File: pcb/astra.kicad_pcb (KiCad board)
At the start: 4 copper layers, 49.2 x 45.5 mm, 93 parts, among them J1 Conn_01x02_Pin, J2 Conn_01x24_MountingPin, J3 Conn_02x04_Odd_Even, J4 Conn_02x05_Odd_Even, M1 Motor_DC, M2 Motor_DC, M3 Motor_DC, M4 Motor_DC, Q1 AO3400A, Q2 AO3400A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

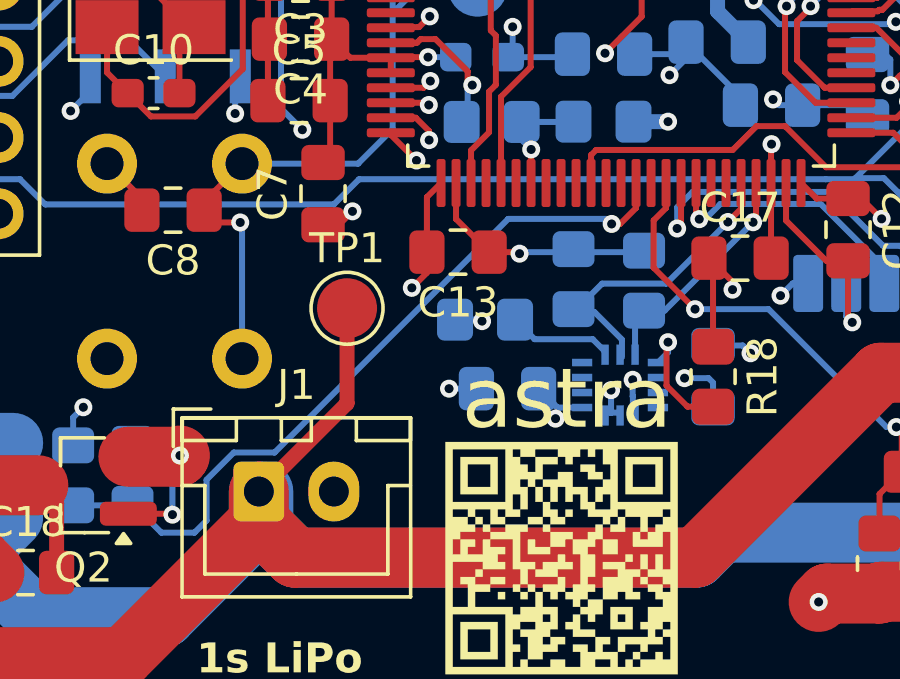
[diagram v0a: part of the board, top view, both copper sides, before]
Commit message: [pcb] add status led
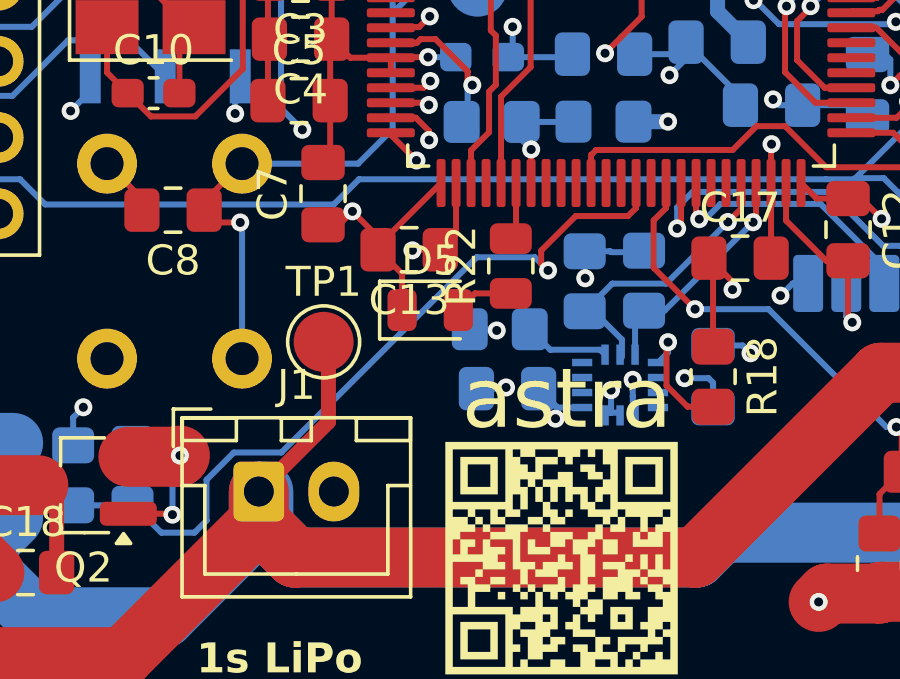
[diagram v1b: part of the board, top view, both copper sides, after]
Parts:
- added D5: LED, LED_SMD:LED_0805_2012Metric, F.Cu at (138.3, 66.6)
- added R22: 1k, Resistor_SMD:R_0805_2012Metric, F.Cu at (141.0, 65.2)
- moved C13 1.63 mm to (137.6, 64.6)
- moved TP1 1.36 mm to (134.7, 67.7)
- moved R19 0.59 mm to (140.6, 67.3)
- moved R17 0.38 mm to (143.4, 65.7)
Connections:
- U3 pad 31: unconnected-(U3-PA7-Pad31) -> STATUS_LED
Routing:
- net GND: track 126.4 -> 129.6 mm, vias 39 -> 38
- net Net-(D5-A): track 0.00 -> 1.98 mm
- net STATUS_LED: track 0.00 -> 1.93 mm
- net +BATT: track 253.5 -> 251.9 mm
- net +3.3V: track 79.6 -> 78.3 mm, vias 24 -> 25
- net MOTOR2: track 25.4 -> 26.4 mm
- net Net-(U7-CSB): track 3.64 -> 2.86 mm
- net IMU_SCL: track 30.1 -> 29.4 mm

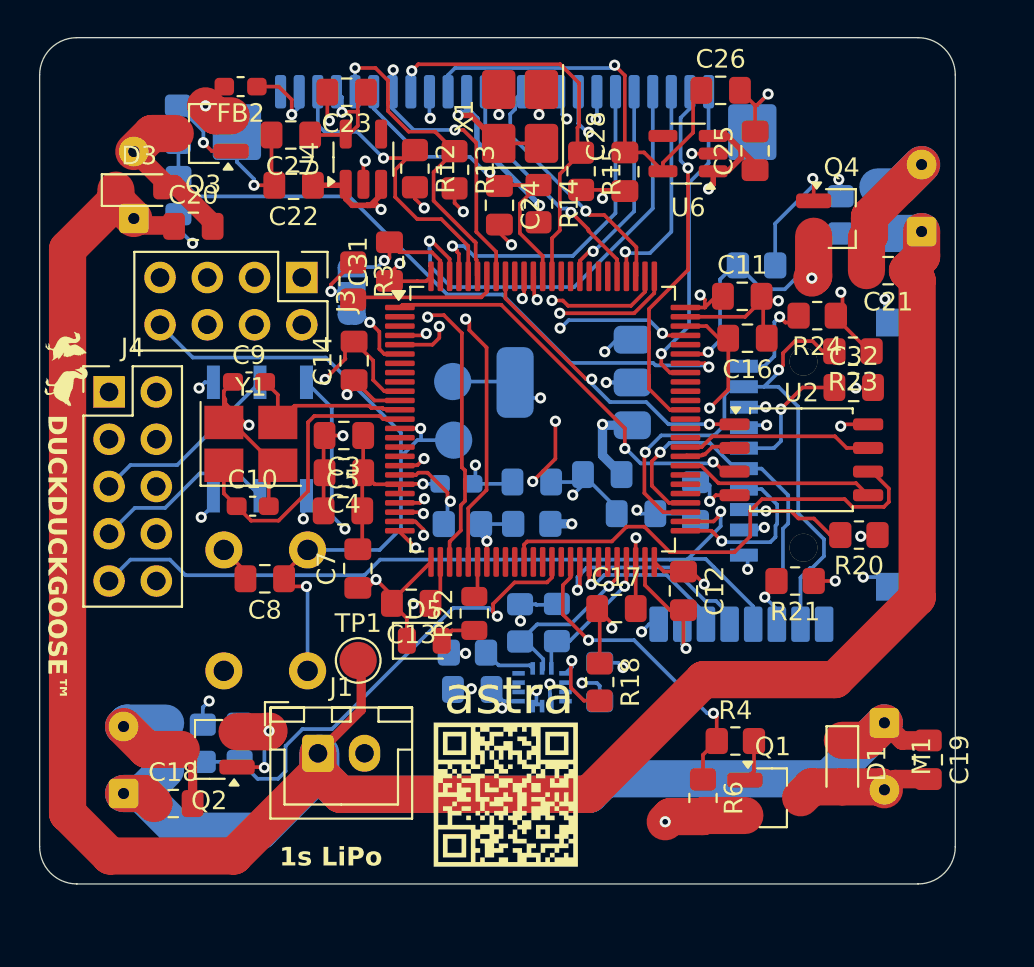
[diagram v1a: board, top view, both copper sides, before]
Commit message: [pcb] small fixes and improvements
- add two status LEDs
- move silkscreen labels for better visibility
- add more silkcreen logos/credits
- fix nrf footprint, add rf keepout zone
- add mounting holes
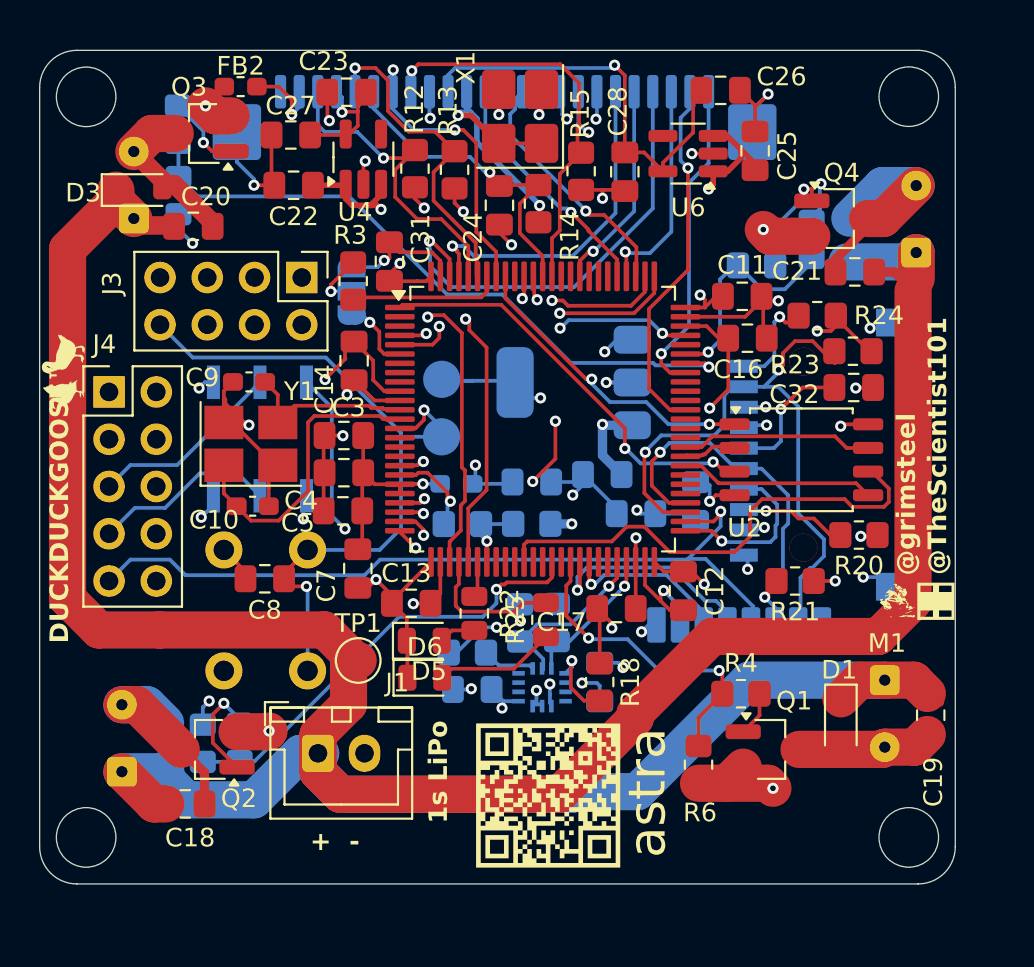
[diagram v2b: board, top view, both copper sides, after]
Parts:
- added D6: LED, LED_SMD:LED_0805_2012Metric, F.Cu at (138.3, 68.6)
- added G***: LOGO, LOGO, F.Cu at (165.8, 64.5)
- added G***: LOGO, LOGO, F.Cu at (163.6, 64.4)
- added G***: LOGO, LOGO, B.Cu at (135.0, 76.5)
- added R25: 1k, Resistor_SMD:R_0805_2012Metric, F.Cu at (144.8, 65.5)
- added REF**: MountingHole_3.2mm_M3, MountingHole:MountingHole_3.2mm_M3, F.Cu at (120.1, 37.4)
- added REF**: MountingHole_3.2mm_M3, MountingHole:MountingHole_3.2mm_M3, F.Cu at (164.3, 77.2)
- added REF**: MountingHole_3.2mm_M3, MountingHole:MountingHole_3.2mm_M3, F.Cu at (120.1, 77.2)
- added REF**: MountingHole_3.2mm_M3, MountingHole:MountingHole_3.2mm_M3, F.Cu at (164.3, 37.4)
- moved Q1 2.60 mm to (156.9, 72.5)
- moved R4 2.56 mm to (155.3, 69.5)
- moved C19 2.40 mm to (165.5, 70.6)
- moved M1 2.29 mm to (163.0, 68.8)
- moved QR***** 2.28 mm to (144.9, 75.0), turned to 90 degrees
- moved D4 2.26 mm to (161.0, 45.0)
- moved D1 2.23 mm to (160.7, 71.0)
- moved R11 2.04 mm to (159.1, 45.1)
- moved G*** 2.00 mm to (142.6, 75.9), turned to 90 degrees
- moved R6 1.81 mm to (153.0, 73.3)
- moved C21 1.79 mm to (161.4, 46.8)
- moved M2 1.17 mm to (122.0, 73.7)
- moved M4 1.17 mm to (164.7, 45.8)
- moved TP3 0.67 mm to (139.2, 55.7)
- moved C18 0.64 mm to (125.4, 75.4)
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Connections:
- net STATUS_LED renamed STATUS_LED_1
- U3 pad 29: unconnected-(U3-PA5-Pad29) -> STATUS_LED_2
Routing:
- net +BATT: track 251.9 -> 241.8 mm
- net STATUS_LED_2: track 0.00 -> 7.60 mm
- net Net-(D6-A): track 0.00 -> 6.48 mm
- net GND: track 129.6 -> 133.7 mm
- net +3.3V: track 78.3 -> 81.6 mm
- net MOTOR2: track 26.4 -> 24.1 mm
- net MOTOR4: track 14.6 -> 12.6 mm
- net Net-(D4-A): track 9.77 -> 11.2 mm
- net Net-(D2-A): track 9.11 -> 10.4 mm
- net Net-(Q2-G): track 4.39 -> 5.66 mm
- net RST: track 39.0 -> 40.1 mm
- net Net-(Q4-G): track 6.73 -> 5.77 mm
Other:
- board size 49.2 x 45.5 mm -> 49.2 x 44.8 mm
- board text added: "+ -"
- board text added: "0123abc"
- board text added: "@TheScientist101"
- board text added: "@grimsteel"
- board text added: "BOOT SELECT"
- board text added: "DDG PERIPHERAL"
- board text added: "I2C"
- board text added: "JLCJLCJLCJLC"
- board text added: "TDO TCK TMS RST"
- board text added: "TRST TDI GND 3V3"
- board text added: "github.com/TheScientist101/astra"
- board text removed: "I²C"

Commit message: [pcb] remove on-board camera
- remove camera and all supporting components (we'll be using an external dedicated board)
- extend DDG header
- make PCB smaller
- add more silkscreen labels
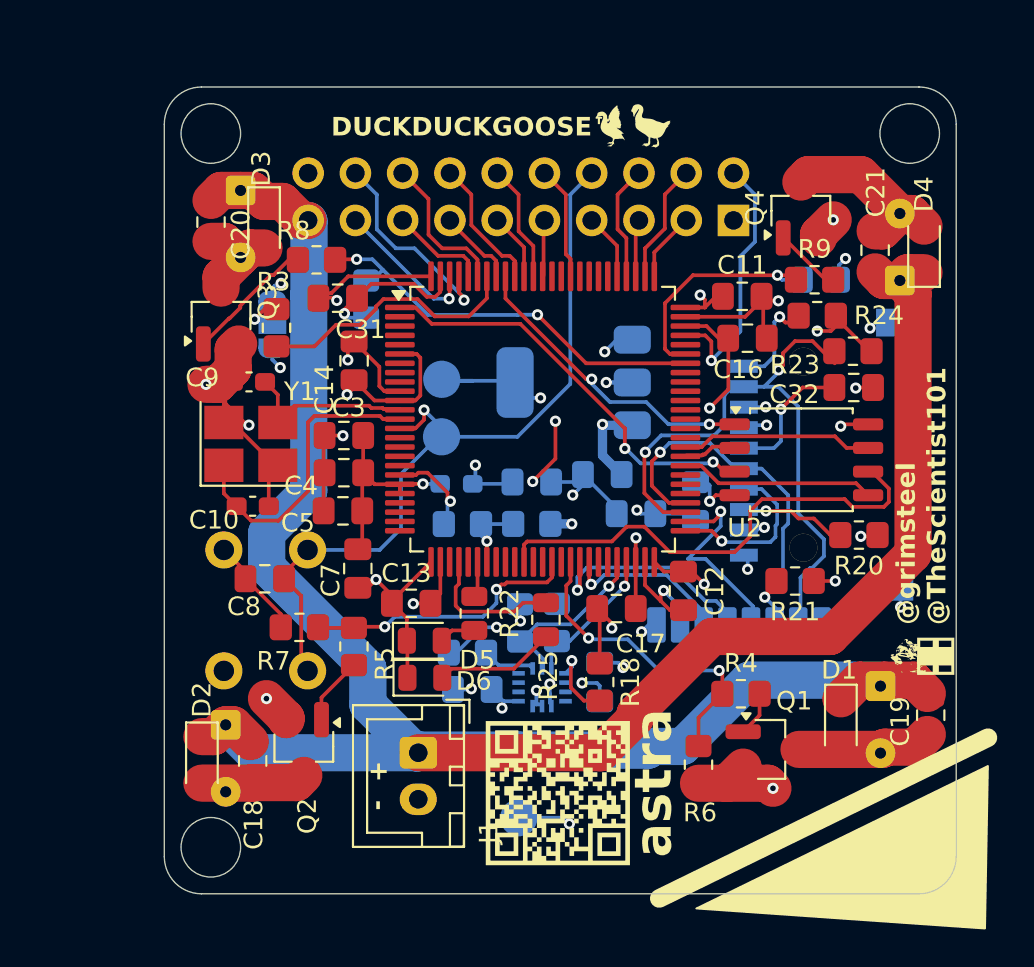
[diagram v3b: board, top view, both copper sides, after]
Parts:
- removed C22: 10uF, Capacitor_SMD:C_0805_2012Metric_Pad1.18x1.45mm_HandSolder
- removed C23, C25, C26: 1uF, Capacitor_SMD:C_0805_2012Metric_Pad1.18x1.45mm_HandSolder
- removed C24, C27, C28: 100nF, Capacitor_SMD:C_0805_2012Metric_Pad1.18x1.45mm_HandSolder
- removed FB2: 121T06, Inductor_SMD:L_0603_1608Metric_Pad1.05x0.95mm_HandSolder
- removed J3: Conn_02x04_Odd_Even, Connector_PinHeader_2.54mm:PinHeader_2x04_P2.54mm_Vertical
- removed J4: Conn_02x05_Odd_Even, Connector_PinHeader_2.54mm:PinHeader_2x05_P2.54mm_Vertical
- removed R12, R13, R14, R15: 10k, Resistor_SMD:R_0805_2012Metric_Pad1.20x1.40mm_HandSolder
- removed SW1: SS-3235S-L1, lcsc:SW-SMD_SS-3235S-LX
- removed U4: TLV74328PDBVR, Package_TO_SOT_SMD:SOT-23-5_HandSoldering
- removed U6: TLV74315PDBVR, Package_TO_SOT_SMD:SOT-23-5_HandSoldering
- removed X1: OT322524MJBA4SL, Crystal:Crystal_SMD_3225-4Pin_3.2x2.5mm_HandSoldering
- added G***: LOGO, LOGO, B.Cu at (157.6, 42.8)
- added GND: TP_GND, TestPoint:TestPoint_Pad_D2.0mm, B.Cu at (143.3, 76.1)
- D2, D4, R5, R7, R8, R9: moved to F.Cu
- J2: value Conn_01x24_MountingPin -> Conn_02x10_Odd_Even; footprint Connector_FFC-FPC:JUSHUO_AFA07-S24FCA-00_1x24-1MP_P1.0mm_Horizontal -> Connector_PinHeader_2.54mm:PinHeader_2x10_P2.54mm_Vertical
- M1: moved to B.Cu
- VCC: renamed from TP1; moved to B.Cu
- moved G*** 33.3 mm to (149.5, 39.0), turned to 0 degrees
- moved G*** 22.1 mm to (130.8, 57.2)
- moved J2 13.3 mm to (154.9, 44.0), turned to 90 degrees
- moved R10 11.5 mm to (135.2, 48.3)
- moved R8 10.4 mm to (132.5, 46.2), turned to 180 degrees
- moved VCC 9.87 mm to (143.3, 72.5), turned to 180 degrees
- moved Q3 9.86 mm to (127.3, 49.2), turned to 90 degrees
- moved R7 8.11 mm to (131.6, 65.9), turned to 180 degrees
- moved R5 8.01 mm to (134.5, 66.9), turned to -90 degrees
- moved REF** 6.98 mm to (126.8, 39.4)
- moved D3 6.96 mm to (129.7, 44.3), turned to -90 degrees
- moved REF** 6.72 mm to (126.8, 77.7)
- moved M2 6.12 mm to (127.6, 71.2), turned to -90 degrees
- moved M3 5.94 mm to (128.4, 42.4), turned to -90 degrees
- moved J1 5.39 mm to (137.9, 72.7), turned to -90 degrees
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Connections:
- J2 pad 1: DCMI_D0 -> GND
- J2 pad 10: GND -> DDG_MAGIC_2
- J2 pad 11: DCMI_D8 -> TRST
- J2 pad 12: DCMI_XCLK -> TDO
- J2 pad 13: DCMI_D9 -> DDG_MAGIC_3
- J2 pad 14: +3.3V -> DDG_MAGIC_4
- J2 pad 15: +1V5 -> I2C1_SDA
- J2 pad 16: DCMI_HSYNC -> I2C1_SCK
- J2 pad 17: DCMI_PWDN -> DDG_MAGIC_5
- J2 pad 18: DCMI_VSYNC -> DDG_MAGIC_6
- J2 pad 19: DCMI_RST -> +BATT
- J2 pad 2: DCMI_D1 -> TMS
- J2 pad 20: DCMI_SCL -> +3.3V
- J2 pad 3: DCMI_D4 -> TCLK
- J2 pad 4: DCMI_D3 -> TDI
- J2 pad 5: DCMI_D5 -> SPI3_CLK
- J2 pad 6: DCMI_D2 -> SPI3_MISO
- J2 pad 7: DCMI_D6 -> SPI3_MOSI
- J2 pad 8: DCMI_PCLK -> RST
- J2 pad 9: DCMI_D7 -> DDG_MAGIC_1
- U3 pad 18: DDG_MAGIC_1 -> unconnected-(U3-PC3_C-Pad18)
- U3 pad 22: DDG_MAGIC_2 -> unconnected-(U3-PA0-Pad22)
- U3 pad 23: DDG_MAGIC_3 -> unconnected-(U3-PA1-Pad23)
- U3 pad 24: DDG_MAGIC_4 -> unconnected-(U3-PA2-Pad24)
- U3 pad 25: DDG_MAGIC_5 -> unconnected-(U3-PA3-Pad25)
- U3 pad 28: DCMI_HSYNC -> unconnected-(U3-PA4-Pad28)
- U3 pad 30: DCMI_PCLK -> unconnected-(U3-PA6-Pad30)
- U3 pad 4: DCMI_D6 -> unconnected-(U3-PE5-Pad4)
- U3 pad 5: DCMI_D7 -> unconnected-(U3-PE6-Pad5)
- U3 pad 64: DCMI_D1 -> unconnected-(U3-PC7-Pad64)
- U3 pad 68: DCMI_D0 -> unconnected-(U3-PA9-Pad68)
- U3 pad 78: DCMI_D8 -> SPI3_CLK
- U3 pad 79: DCMI_D4 -> SPI3_MISO
- U3 pad 80: DCMI_D9 -> SPI3_MOSI
- U3 pad 84: DCMI_D5 -> unconnected-(U3-PD3-Pad84)
- U3 pad 85: unconnected-(U3-PD4-Pad85) -> DDG_MAGIC_2
- U3 pad 87: DCMI_PWDN -> unconnected-(U3-PD6-Pad87)
- U3 pad 88: DCMI_RST -> DDG_MAGIC_1
- U3 pad 91: unconnected-(U3-PB5-Pad91) -> DDG_MAGIC_4
- U3 pad 93: DCMI_VSYNC -> DDG_MAGIC_3
- U3 pad 95: DCMI_SCL -> I2C1_SCK
- U3 pad 96: DCMI_SDA -> I2C1_SDA
- U3 pad 97: DCMI_D2 -> DDG_MAGIC_6
- U3 pad 98: DCMI_D3 -> DDG_MAGIC_5
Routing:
- net +BATT: track 241.8 -> 163.7 mm, vias 4 -> 2
- net SPI2_CLK: track 51.4 -> 18.4 mm
- net SPI2_MISO: track 66.0 -> 34.0 mm, vias 3 -> 2
- net SPI2_MOSI: track 50.8 -> 19.4 mm, vias 3 -> 2
- net GND: track 133.7 -> 102.6 mm, vias 38 -> 30
- net DCMI_PCLK: track 29.5 -> 0.00 mm, vias 2 -> 0
- net DCMI_HSYNC: track 28.1 -> 0.00 mm, vias 2 -> 0
- net IMU_SDA: track 34.0 -> 7.46 mm, vias 2 -> 1
- net DCMI_D3: track 24.2 -> 0.00 mm, vias 1 -> 0
- net +1V5: track 22.7 -> 0.00 mm, vias 1 -> 0
- net TCLK: track 25.6 -> 3.72 mm, vias 1 -> 0
- net DCMI_PWDN: track 21.9 -> 0.00 mm, vias 1 -> 0
- net TDI: track 26.9 -> 6.46 mm, vias 1 -> 0
- net IMU_SCL: track 29.4 -> 9.41 mm, vias 2 -> 1
- net DCMI_D1: track 19.6 -> 0.00 mm, vias 1 -> 0
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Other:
- board size 49.2 x 44.8 mm -> 42.6 x 43.4 mm
- board text added: "B5"
- board text added: "B7"
- board text added: "BOOT"
- board text added: "D4"
- board text added: "D7"
- board text added: "E0"
- board text added: "E1"
- board text added: "GND"
- board text added: "MISO"
- board text added: "MO"
- board text added: "SCK"
- board text added: "SDA"
- board text added: "SYS USR"
- board text added: "TCK"
- board text added: "TDI"
- board text added: "TDO"
- board text added: "TMS"
- board text added: "TRS"
- board text added: "VCC"
- board text removed: "1s LiPo"
- board text removed: "BOOT SELECT"
- board text removed: "DDG PERIPHERAL"
- board text removed: "I2C"
- board text removed: "SPI"
- board text removed: "TDO TCK TMS RST"
- board text removed: "TRST TDI GND 3V3"
